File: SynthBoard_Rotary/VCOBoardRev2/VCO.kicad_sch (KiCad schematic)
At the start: 51 parts, among them IC1 AS321KTR-E1, IC2 V3340M

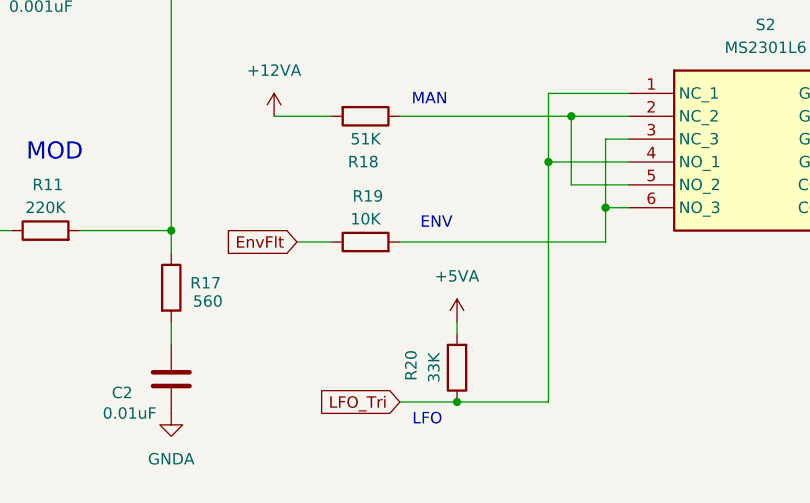
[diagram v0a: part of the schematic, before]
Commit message: MC2 Synth-Board Rotary
V0.2
U10:PIn4 -12Vに接続
IC4:Pin12,13 デフォルト12でジャンパーパッドを追加
R86:三角波をS2に未接続だったのを修正
S2,S3:スイッチ動作を上下入れ替え
VR9:右に2.5mm移動に伴い周辺回路の配置を変更
冗長な配線を修正
ビアを打った
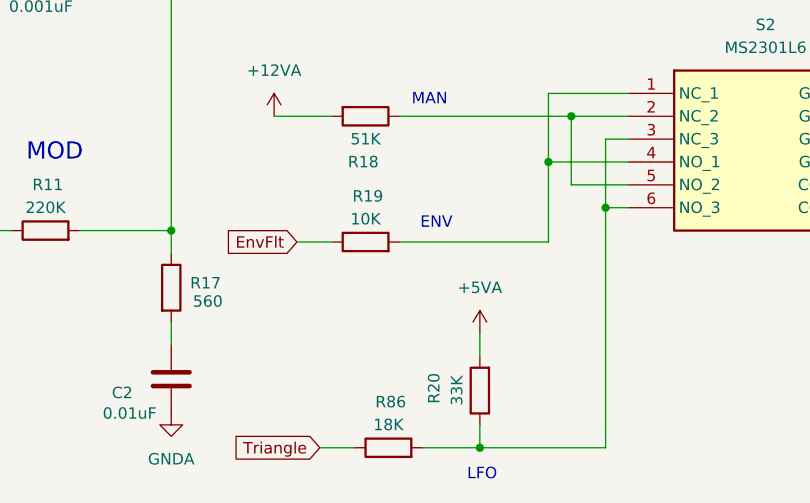
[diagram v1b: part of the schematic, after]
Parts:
- added R86: 18K, Resistor_THT:R_Axial_DIN0207_L6.3mm_D2.5mm_P2.54mm_Vertical, symbol Device:R
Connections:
- net at S2.3 (NC_3), S2.6 (NO_3): now also R20.1, R86.2; no longer R19.2
- net LFO_Tri: no longer names the net of S2.1 (NC_1), S2.4 (NO_1)
- net LFO_Tri: now also R19.2; no longer R20.1
- new net Triangle: R86.1
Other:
- moved on the sheet: R20
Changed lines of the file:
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@@
 	(text "LFO"
 		(exclude_from_sim no)
-		(at 136.398 184.912 0)
+		(at 142.494 191.008 0)
 		(effects
 			(font
@@
 	)
 	(junction
-		(at 139.7 182.88)
+		(at 107.95 81.28)
 		(diameter 0)
 		(color 0 0 0 0)
 	)
 	(junction
-		(at 107.95 81.28)
+		(at 237.49 48.26)
 		(diameter 0)
 		(color 0 0 0 0)
 	)
 	(junction
-		(at 237.49 48.26)
+		(at 194.31 148.59)
 		(diameter 0)
 		(color 0 0 0 0)
 	)
 	(junction
-		(at 194.31 148.59)
+		(at 156.21 161.29)
 		(diameter 0)
 		(color 0 0 0 0)
@@
 	)
 	(junction
-		(at 156.21 161.29)
+		(at 142.24 187.96)
 		(diameter 0)
 		(color 0 0 0 0)
@@
 	)
 	(junction
+		(at 149.86 156.21)
+		(diameter 0)
+		(color 0 0 0 0)
+	)
+	(junction
 		(at 86.36 133.35)
 		(diameter 0)
@@
 		(color 0 0 0 0)
 	)
-	(junction
-		(at 149.86 156.21)
-		(diameter 0)
-		(color 0 0 0 0)
-	)
 	(no_connect
 		(at 93.98 85.09)
@@
 	(wire
 		(pts
-			(xy 149.86 182.88) (xy 149.86 156.21)
+			(xy 156.21 187.96) (xy 156.21 161.29)
 		)
 		(stroke
@@
 	(wire
 		(pts
-			(xy 29.21 82.55) (xy 34.29 82.55)
+			(xy 135.89 187.96) (xy 142.24 187.96)
 		)
 		(stroke
@@
 	(wire
 		(pts
-			(xy 97.79 163.83) (xy 107.95 163.83)
+			(xy 29.21 82.55) (xy 34.29 82.55)
 		)
 		(stroke
@@
 	(wire
 		(pts
-			(xy 189.23 153.67) (xy 194.31 153.67)
+			(xy 97.79 163.83) (xy 107.95 163.83)
 		)
 		(stroke
@@
 	(wire
 		(pts
-			(xy 176.53 46.99) (xy 167.64 46.99)
+			(xy 189.23 153.67) (xy 194.31 153.67)
 		)
 		(stroke
@@
 	(wire
 		(pts
-			(xy 189.23 158.75) (xy 193.04 158.75)
+			(xy 176.53 46.99) (xy 167.64 46.99)
 		)
 		(stroke
@@
 	(wire
 		(pts
-			(xy 241.3 71.12) (xy 241.3 72.39)
+			(xy 189.23 158.75) (xy 193.04 158.75)
 		)
 		(stroke
@@
 	(wire
 		(pts
-			(xy 158.75 153.67) (xy 156.21 153.67)
+			(xy 241.3 71.12) (xy 241.3 72.39)
 		)
 		(stroke
@@
 	(wire
 		(pts
-			(xy 104.14 102.87) (xy 107.95 102.87)
+			(xy 158.75 153.67) (xy 156.21 153.67)
 		)
 		(stroke
@@
 	(wire
 		(pts
-			(xy 133.35 182.88) (xy 139.7 182.88)
+			(xy 104.14 102.87) (xy 107.95 102.87)
 		)
 		(stroke
@@
 	(wire
 		(pts
-			(xy 139.7 182.88) (xy 149.86 182.88)
-		)
-		(stroke
-			(width 0)
-			(type default)
-		)
-	)
-	(wire
-		(pts
 			(xy 176.53 49.53) (xy 176.53 46.99)
 		)
@@
 	(wire
 		(pts
-			(xy 156.21 165.1) (xy 156.21 161.29)
-		)
-		(stroke
-			(width 0)
-			(type default)
-		)
-	)
-	(wire
-		(pts
 			(xy 156.21 153.67) (xy 156.21 161.29)
 		)
@@
 	(wire
 		(pts
+			(xy 133.35 165.1) (xy 149.86 165.1)
+		)
+		(stroke
+			(width 0)
+			(type default)
+		)
+	)
+	(wire
+		(pts
 			(xy 52.07 55.88) (xy 49.53 55.88)
 		)
@@
 	(wire
 		(pts
+			(xy 142.24 187.96) (xy 156.21 187.96)
+		)
+		(stroke
+			(width 0)
+			(type default)
+		)
+	)
+	(wire
+		(pts
 			(xy 194.31 151.13) (xy 194.31 148.59)
 		)
@@
 	(wire
 		(pts
-			(xy 245.11 101.6) (xy 240.03 101.6)
+			(xy 124.46 187.96) (xy 128.27 187.96)
 		)
 		(stroke
@@
 	(wire
 		(pts
-			(xy 220.98 120.65) (xy 224.79 120.65)
+			(xy 245.11 101.6) (xy 240.03 101.6)
 		)
 		(stroke
@@
 	(wire
 		(pts
-			(xy 133.35 165.1) (xy 156.21 165.1)
+			(xy 220.98 120.65) (xy 224.79 120.65)
 		)
 		(stroke
@@
 	(wire
 		(pts
-			(xy 139.7 173.99) (xy 139.7 175.26)
+			(xy 142.24 175.26) (xy 142.24 177.8)
+		)
+		(stroke
+			(width 0)
+			(type default)
+		)
+	)
+	(wire
+		(pts
+			(xy 142.24 185.42) (xy 142.24 187.96)
 		)
 		(stroke
@@
 	(wire
 		(pts
+			(xy 149.86 165.1) (xy 149.86 156.21)
+		)
+		(stroke
+			(width 0)
+			(type default)
+		)
+	)
+	(wire
+		(pts
 			(xy 240.03 110.49) (xy 240.03 113.03)
 		)
@@
 		)
 	)
+	(global_label "Triangle"
+		(shape input)
+		(at 124.46 187.96 180)
+		(fields_autoplaced yes)
+		(effects
+			(font
+				(size 1.27 1.27)
+			)
+			(justify right)
+		)
+		(property "Intersheetrefs" "${INTERSHEET_REFS}"
+			(at 113.9154 187.96 0)
+			(effects
+				(font
+					(size 1.27 1.27)
+				)
+				(justify right)
+				(hide yes)
+			)
+		)
+	)
 	(global_label "S5_A_2"
 		(shape input)
@@
 		)
 	)
-	(global_label "LFO_Tri"
-		(shape input)
-		(at 133.35 182.88 180)
-		(fields_autoplaced yes)
-		(effects
-			(font
-				(size 1.27 1.27)
-			)
-			(justify right)
-		)
-		(property "Intersheetrefs" "${INTERSHEET_REFS}"
-			(at 126.8571 182.88 0)
-			(effects
-				(font
-					(size 1.27 1.27)
-				)
-				(justify right)
-				(hide yes)
-			)
-		)
-	)
 	(global_label "VP"
 		(shape output)
@@
 	(symbol
 		(lib_id "power:+5VA")
-		(at 139.7 173.99 0)
+		(at 142.24 175.26 0)
 		(unit 1)
 		(exclude_from_sim no)
@@
 		(on_board yes)
 		(dnp no)
-		(fields_autoplaced yes)
 		(property "Reference" "#PWR017"
-			(at 139.7 177.8 0)
+			(at 142.24 179.07 0)
 			(effects
 				(font
@@
 		)
 		(property "Value" "+5VA"
-			(at 139.7 168.91 0)
+			(at 142.24 170.18 0)
 			(effects
 				(font
@@
 		)
 		(property "Footprint" ""
-			(at 139.7 173.99 0)
+			(at 142.24 175.26 0)
 			(effects
 				(font
@@
 		)
 		(property "Datasheet" ""
-			(at 139.7 173.99 0)
+			(at 142.24 175.26 0)
 			(effects
 				(font
@@
 		)
 		(property "Description" "Power symbol creates a global label with name \"+5VA\""
-			(at 139.7 173.99 0)
+			(at 142.24 175.26 0)
 			(effects
 				(font
@@
 	(symbol
 		(lib_id "Device:R")
-		(at 139.7 179.07 180)
+		(at 142.24 181.61 180)
 		(unit 1)
 		(exclude_from_sim no)
@@
 		(dnp no)
 		(property "Reference" "R20"
-			(at 134.62 178.816 90)
+			(at 137.16 181.356 90)
 			(effects
 				(font
@@
 		)
 		(property "Value" "33K"
-			(at 137.16 179.07 90)
+			(at 139.7 181.61 90)
 			(effects
 				(font
@@
 		)
 		(property "Footprint" "Resistor_THT:R_Axial_DIN0207_L6.3mm_D2.5mm_P2.54mm_Vertical"
-			(at 141.478 179.07 90)
+			(at 144.018 181.61 90)
 			(effects
 				(font
@@
 		)
 		(property "Datasheet" "~"
-			(at 139.7 179.07 0)
+			(at 142.24 181.61 0)
 			(effects
 				(font
@@
 		)
 		(property "Description" "Resistor"
-			(at 139.7 179.07 0)
+			(at 142.24 181.61 0)
 			(effects
 				(font
@@
 		)
 		(property "Sim.Library" ""
-			(at 139.7 179.07 90)
+			(at 142.24 181.61 90)
 			(effects
 				(font
@@
 		)
 		(property "Sim.Name" ""
-			(at 139.7 179.07 90)
+			(at 142.24 181.61 90)
 			(effects
 				(font
@@
 					(unit 1)
 				)
+			)
+		)
+	)
+	(symbol
+		(lib_id "Device:R")
+		(at 132.08 187.96 90)
+		(unit 1)
+		(exclude_from_sim no)
+		(in_bom yes)
+		(on_board yes)
+		(dnp no)
+		(property "Reference" "R86"
+			(at 132.334 182.88 90)
+			(effects
+				(font
+					(size 1.27 1.27)
+				)
+			)
+		)
+		(property "Value" "18K"
+			(at 132.08 185.42 90)
+			(effects
+				(font
+					(size 1.27 1.27)
+				)
+			)
+		)
+		(property "Footprint" "Resistor_THT:R_Axial_DIN0207_L6.3mm_D2.5mm_P2.54mm_Vertical"
+			(at 132.08 189.738 90)
+			(effects
+				(font
+					(size 1.27 1.27)
+				)
+				(hide yes)
+			)
+		)
+		(property "Datasheet" "~"
+			(at 132.08 187.96 0)
+			(effects
+				(font
+					(size 1.27 1.27)
+				)
+				(hide yes)
+			)
+		)
+		(property "Description" "Resistor"
+			(at 132.08 187.96 0)
+			(effects
+				(font
+					(size 1.27 1.27)
+				)
+				(hide yes)
+			)
+		)
+		(property "Sim.Library" ""
+			(at 132.08 187.96 90)
+			(effects
+				(font
+					(size 1.27 1.27)
+				)
+				(hide yes)
+			)
+		)
+		(property "Sim.Name" ""
+			(at 132.08 187.96 90)
+			(effects
+				(font
+					(size 1.27 1.27)
+				)
+				(hide yes)
+			)
+		)
+		(pin "1"
+		)
+		(pin "2"
+		)
+		(instances
+			(project "VCOSeparate"
+				(path "/bae8314b-242c-4fa4-bbce-99492909575e/2f41abe6-7163-4fa2-8be9-b46ea312e2c4"
+					(reference "R86")
+					(unit 1)
+				)
